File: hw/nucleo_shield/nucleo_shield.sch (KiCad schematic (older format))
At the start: 26 parts, among them CN101 Nucleo-F411RE-CN10, CN71 Nucleo-F411RE-CN7, P1 CONN_01X10, P2 CONN_01X10, P3 CONN_01X10, P4 CONN_01X02, U1 74HC595, U2 74HC595, U3 LTV-847, U4 LTV-847

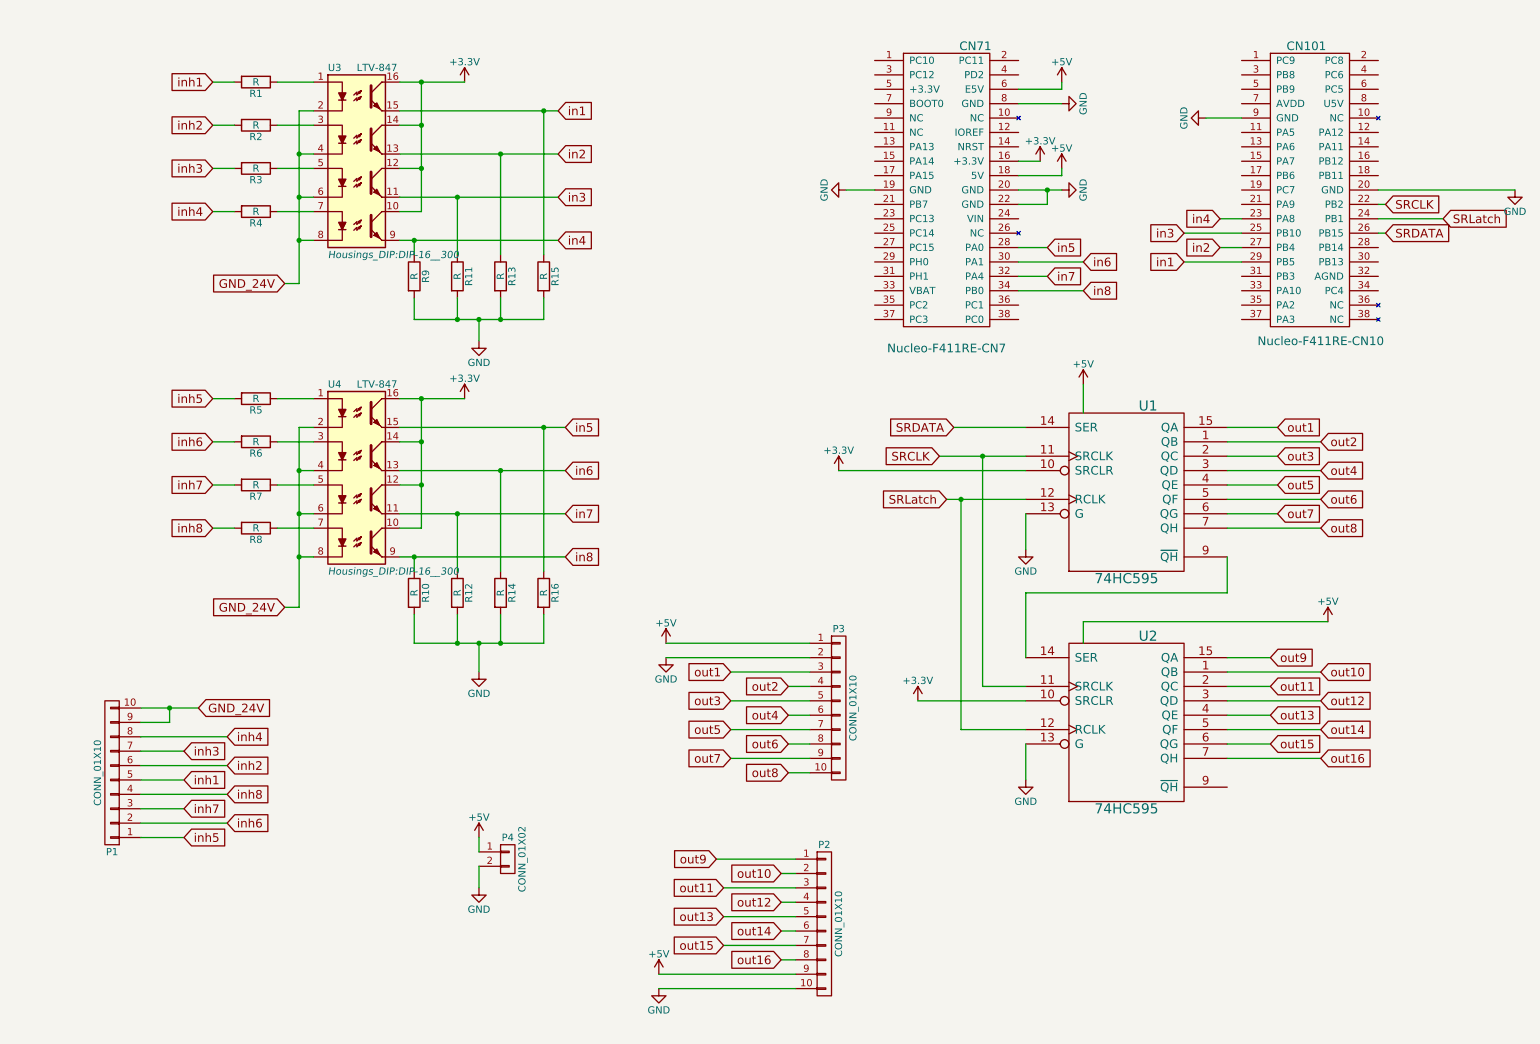
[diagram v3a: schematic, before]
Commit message: Nucleo: add 4 more inputs
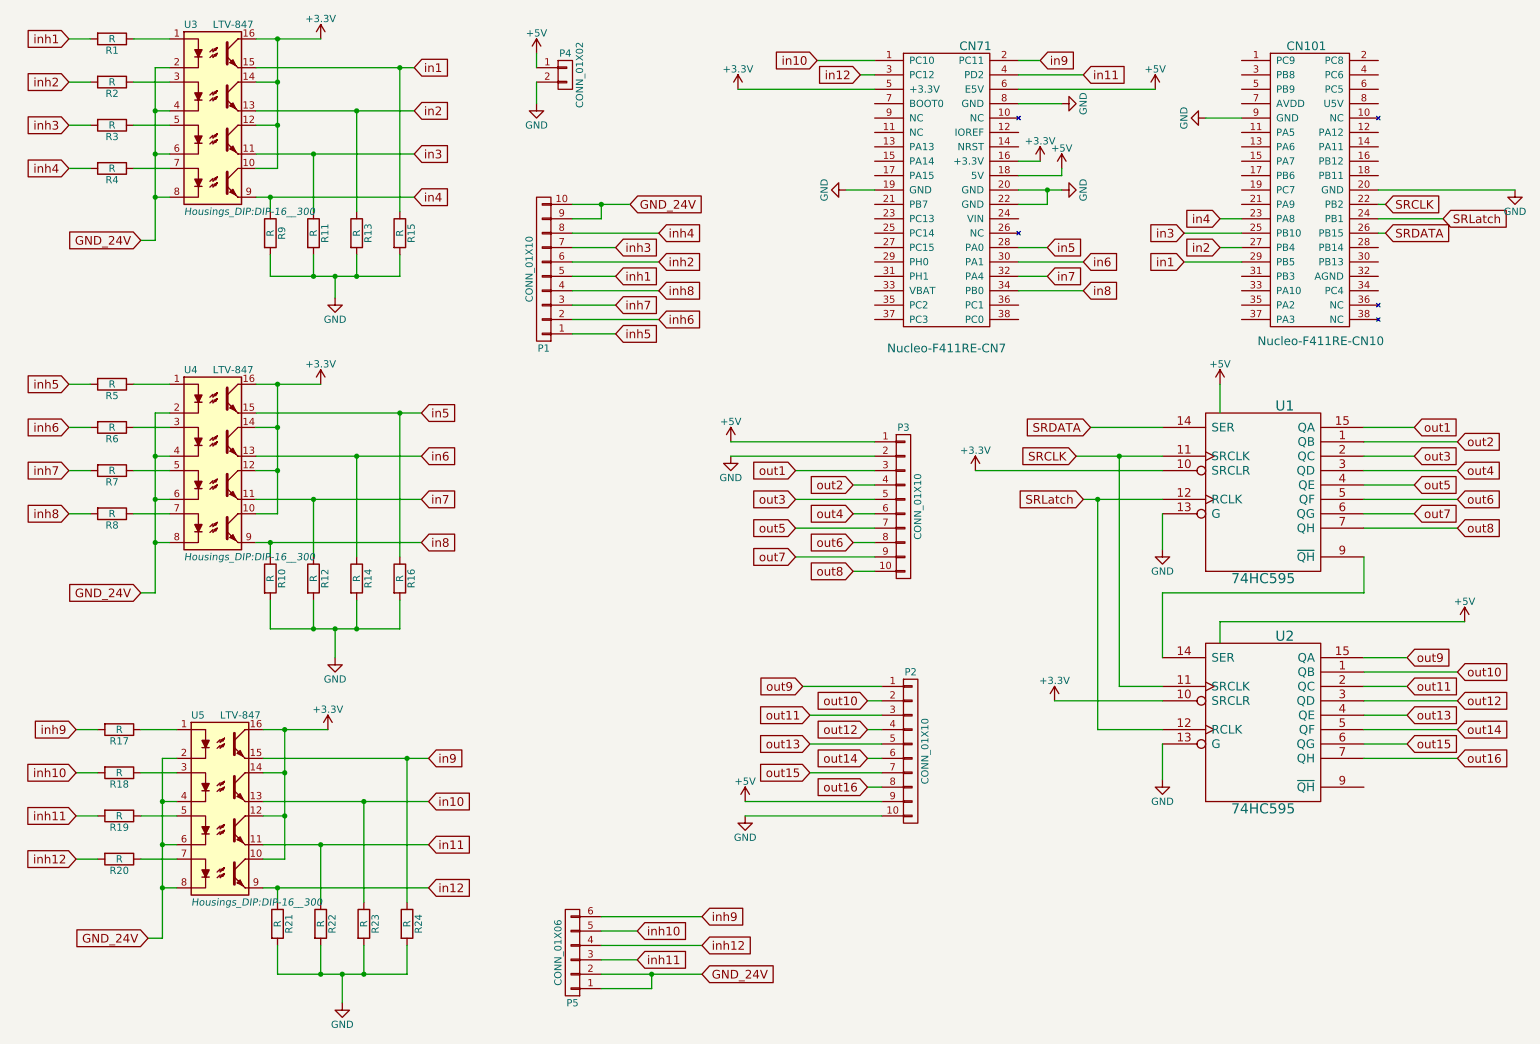
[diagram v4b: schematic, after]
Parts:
- added P5: CONN_01X06, w_conn_screw:mors_6p, symbol CONN_01X06
- added R17, R18, R19, R20, R21, R22, R23, R24: R, Resistors_ThroughHole:Resistor_Horizontal_RM10mm, symbol R
- added U5: LTV-847, Housings_DIP:DIP-16__300, symbol LTV-847
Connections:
- net +3V3: now also CN71.5 (+3.3V), U5.10, U5.12, U5.14, U5.16
- net GND: now also R21.2, R22.2, R23.2, R24.2
- net GND_24V: now also P5.1 (P1), P5.2 (P2), U5.2, U5.4, U5.6, U5.8
- net in10: now reaches CN71.1 (PC10)
- net in10: now also R23.1, U5.13
- net in9: now reaches CN71.2 (PC11)
- net in9: now also R24.1, U5.15
- net in12: now reaches CN71.3 (PC12)
- net in12: now also R21.1, U5.9
- net in11: now reaches CN71.4 (PD2)
- net in11: now also R22.1, U5.11
- new net: R17.1, U5.1
- new net: R18.1, U5.3
- new net: R19.1, U5.5
- new net: R20.1, U5.7
- new net inh10: P5.5 (P5), R18.2
- new net inh11: P5.3 (P3), R19.2
- new net inh12: P5.4 (P4), R20.2
- new net inh9: P5.6 (P6), R17.2
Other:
- moved on the sheet: P1, P2, P3, P4, R1, R10, R11, R12, R13, R14, R15, R16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

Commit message: Nucleo: small modifications for larger ground plan
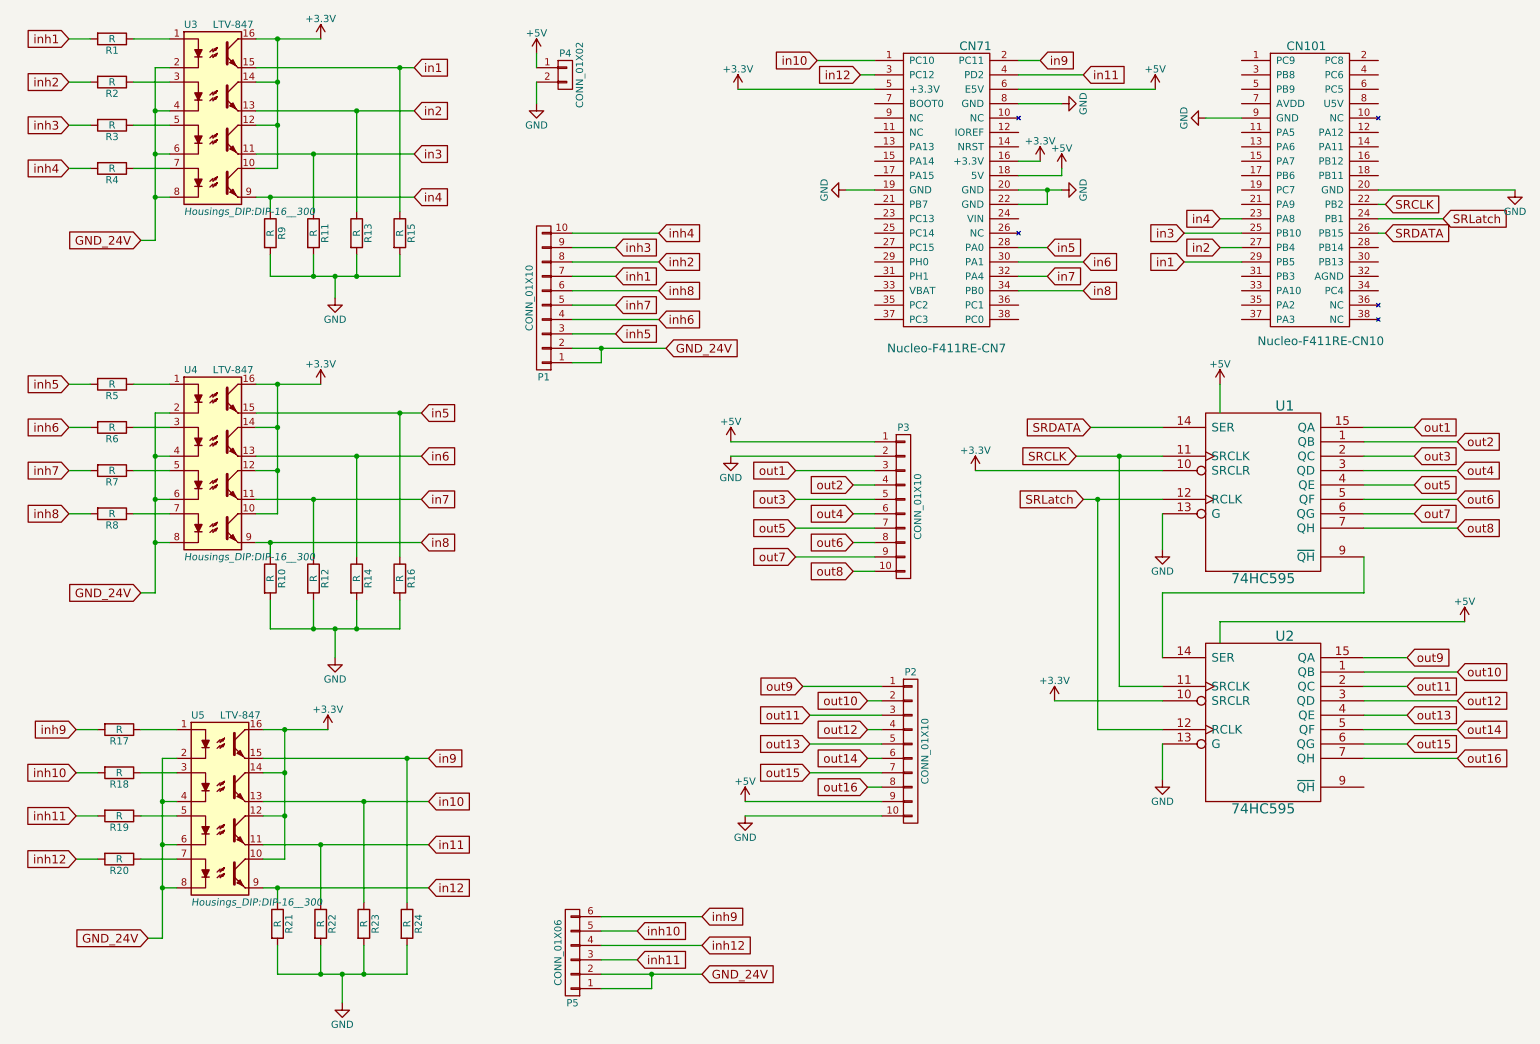
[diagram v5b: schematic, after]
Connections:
- net GND_24V: now also P1.1 (P1), P1.2 (P2); no longer P1.10 (P10), P1.9 (P9)
- net inh1: now also P1.7 (P7); no longer P1.5 (P5)
- net inh2: now also P1.8 (P8); no longer P1.6 (P6)
- net inh3: now also P1.9 (P9); no longer P1.7 (P7)
- net inh4: now also P1.10 (P10); no longer P1.8 (P8)
- net inh5: now also P1.3 (P3); no longer P1.1 (P1)
- net inh6: now also P1.4 (P4); no longer P1.2 (P2)
- net inh7: now also P1.5 (P5); no longer P1.3 (P3)
- net inh8: now also P1.6 (P6); no longer P1.4 (P4)
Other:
- moved on the sheet: P1
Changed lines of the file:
@@
 Text GLabel 1500 4650 0    60   Input ~ 0
 GND_24V
-Text GLabel 4900 1950 2    60   Input ~ 0
+Text GLabel 5150 2950 2    60   Input ~ 0
 GND_24V
 Text GLabel 4800 2450 2    60   Input ~ 0
@@
 	8600 5700 8600 5950
 Wire Wire Line
-	8050 4000 8600 4000
+	8050 4000 8150 4000
+Wire Wire Line
+	8150 4000 8600 4000
 Connection ~ 8150 4000
 Wire Wire Line
@@
 	8150 5600 8600 5600
 Wire Wire Line
-	8000 3700 8600 3700
+	8000 3700 8300 3700
+Wire Wire Line
+	8300 3700 8600 3700
 Connection ~ 8300 3700
 Wire Wire Line
@@
 	10100 1850 11050 1850
 Wire Wire Line
-	2300 1000 3400 1000
-Wire Wire Line
-	2300 1300 3400 1300
-Wire Wire Line
-	2300 1600 3400 1600
-Wire Wire Line
-	2300 1900 3400 1900
-Wire Wire Line
-	2300 3400 3450 3400
-Wire Wire Line
-	2300 3700 3450 3700
-Wire Wire Line
-	2300 4000 3450 4000
-Wire Wire Line
-	2300 4300 3450 4300
+	2300 1000 3300 1000
+Wire Wire Line
+	3300 1000 3400 1000
+Wire Wire Line
+	2300 1300 3000 1300
+Wire Wire Line
+	3000 1300 3400 1300
+Wire Wire Line
+	2300 1600 2700 1600
+Wire Wire Line
+	2700 1600 3400 1600
+Wire Wire Line
+	2300 1900 2400 1900
+Wire Wire Line
+	2400 1900 3400 1900
+Wire Wire Line
+	2300 3400 3300 3400
+Wire Wire Line
+	3300 3400 3450 3400
+Wire Wire Line
+	2300 3700 3000 3700
+Wire Wire Line
+	3000 3700 3450 3700
+Wire Wire Line
+	2300 4000 2700 4000
+Wire Wire Line
+	2700 4000 3450 4000
+Wire Wire Line
+	2300 4300 2400 4300
+Wire Wire Line
+	2400 4300 3450 4300
 Wire Wire Line
 	10000 5100 10300 5100
@@
 	2400 4700 2400 4900
 Wire Wire Line
-	2400 4900 3300 4900
+	2400 4900 2700 4900
+Wire Wire Line
+	2700 4900 2850 4900
+Wire Wire Line
+	2850 4900 3000 4900
+Wire Wire Line
+	3000 4900 3300 4900
 Wire Wire Line
 	2700 4900 2700 4700
@@
 	2400 2300 2400 2450
 Wire Wire Line
-	2400 2450 3300 2450
+	2400 2450 2700 2450
+Wire Wire Line
+	2700 2450 2850 2450
+Wire Wire Line
+	2850 2450 3000 2450
+Wire Wire Line
+	3000 2450 3300 2450
 Wire Wire Line
 	3300 2450 3300 2300
@@
 	1600 1900 1700 1900
 Wire Wire Line
-	1600 1000 1600 2200
+	1600 1000 1600 1300
+Wire Wire Line
+	1600 1300 1600 1600
+Wire Wire Line
+	1600 1600 1600 1900
+Wire Wire Line
+	1600 1900 1600 2200
 Wire Wire Line
 	1700 1600 1600 1600
@@
 	1600 4300 1700 4300
 Wire Wire Line
-	1600 3400 1600 4650
+	1600 3400 1600 3700
+Wire Wire Line
+	1600 3700 1600 4000
+Wire Wire Line
+	1600 4000 1600 4300
+Wire Wire Line
+	1600 4300 1600 4650
 Wire Wire Line
 	1700 4000 1600 4000
@@
 	9150 1350 8900 1350
 Wire Wire Line
-	2300 800  2750 800
-Wire Wire Line
-	2450 800  2450 1700
+	2300 800  2450 800
+Wire Wire Line
+	2450 800  2750 800
+Wire Wire Line
+	2450 800  2450 1100
+Wire Wire Line
+	2450 1100 2450 1400
+Wire Wire Line
+	2450 1400 2450 1700
 Wire Wire Line
 	2450 1700 2300 1700
@@
 Connection ~ 2450 1100
 Wire Wire Line
-	2300 3200 2750 3200
+	2300 3200 2450 3200
+Wire Wire Line
+	2450 3200 2750 3200
 Wire Wire Line
 	2450 4100 2300 4100
 Wire Wire Line
-	2450 3200 2450 4100
+	2450 3200 2450 3500
+Wire Wire Line
+	2450 3500 2450 3800
+Wire Wire Line
+	2450 3800 2450 4100
 Connection ~ 2450 3200
 Wire Wire Line
@@
 L CONN_01X10 P1
 U 1 1 56A91B4E
-P 4300 2400
-F 0 "P1" H 4300 2950 50  0000 C CNN
-F 1 "CONN_01X10" V 4400 2400 50  0000 C CNN
-F 2 "w_conn_screw:mors_10p" H 4300 2400 60  0001 C CNN
-F 3 "" H 4300 2400 60  0000 C CNN
-	1    4300 2400
+P 4300 2600
+F 0 "P1" H 4300 3150 50  0000 C CNN
+F 1 "CONN_01X10" V 4400 2600 50  0000 C CNN
+F 2 "w_conn_screw:mors_10p" H 4300 2600 60  0001 C CNN
+F 3 "" H 4300 2600 60  0000 C CNN
+	1    4300 2600
 	-1   0    0    1
 $EndComp
 Wire Wire Line
-	4500 1950 4900 1950
+	4500 2950 4700 2950
+Wire Wire Line
+	4700 2950 5150 2950
 $Comp
 L GND #PWR09
@@
 inh5
 Wire Wire Line
-	4500 2050 4700 2050
-Wire Wire Line
-	4700 2050 4700 1950
-Connection ~ 4700 1950
+	4500 3050 4700 3050
+Wire Wire Line
+	4700 3050 4700 2950
+Connection ~ 4700 2950
 $Comp
 L +5V #PWR013
@@
 	7800 1950 7800 1850
 Wire Wire Line
-	7600 1850 7900 1850
+	7600 1850 7800 1850
+Wire Wire Line
+	7800 1850 7900 1850
 Connection ~ 7800 1850
 $Comp
@@
 GND_24V
 Wire Wire Line
-	2350 5800 3500 5800
-Wire Wire Line
-	2350 6100 3500 6100
-Wire Wire Line
-	2350 6400 3500 6400
-Wire Wire Line
-	2350 6700 3500 6700
+	2350 5800 3350 5800
+Wire Wire Line
+	3350 5800 3500 5800
+Wire Wire Line
+	2350 6100 3050 6100
+Wire Wire Line
+	3050 6100 3500 6100
+Wire Wire Line
+	2350 6400 2750 6400
+Wire Wire Line
+	2750 6400 3500 6400
+Wire Wire Line
+	2350 6700 2450 6700
+Wire Wire Line
+	2450 6700 3500 6700
 Wire Wire Line
 	2450 6800 2450 6700
@@
 	2450 7100 2450 7300
 Wire Wire Line
-	2450 7300 3350 7300
+	2450 7300 2750 7300
+Wire Wire Line
+	2750 7300 2900 7300
+Wire Wire Line
+	2900 7300 3050 7300
+Wire Wire Line
+	3050 7300 3350 7300
 Wire Wire Line
 	2750 7300 2750 7100
@@
 	1650 6700 1750 6700
 Wire Wire Line
-	1650 5800 1650 7050
+	1650 5800 1650 6100
+Wire Wire Line
+	1650 6100 1650 6400
+Wire Wire Line
+	1650 6400 1650 6700
+Wire Wire Line
+	1650 6700 1650 7050
 Wire Wire Line
 	1750 6400 1650 6400
@@
 Connection ~ 1650 6100
 Wire Wire Line
-	2350 5600 2800 5600
+	2350 5600 2500 5600
+Wire Wire Line
+	2500 5600 2800 5600
 Wire Wire Line
 	2500 6500 2350 6500
 Wire Wire Line
-	2500 5600 2500 6500
+	2500 5600 2500 5900
+Wire Wire Line
+	2500 5900 2500 6200
+Wire Wire Line
+	2500 6200 2500 6500
 Connection ~ 2500 5600
 Wire Wire Line
@@
 	4700 7200 4950 7200
 Wire Wire Line
-	4700 7300 5400 7300
+	4700 7300 5050 7300
+Wire Wire Line
+	5050 7300 5400 7300
 Wire Wire Line
 	4700 7400 5050 7400
